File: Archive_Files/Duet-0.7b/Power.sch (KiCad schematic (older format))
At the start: 22 parts, among them U2 TC2117-3.3VDBTR, U3 MC7805CDTG

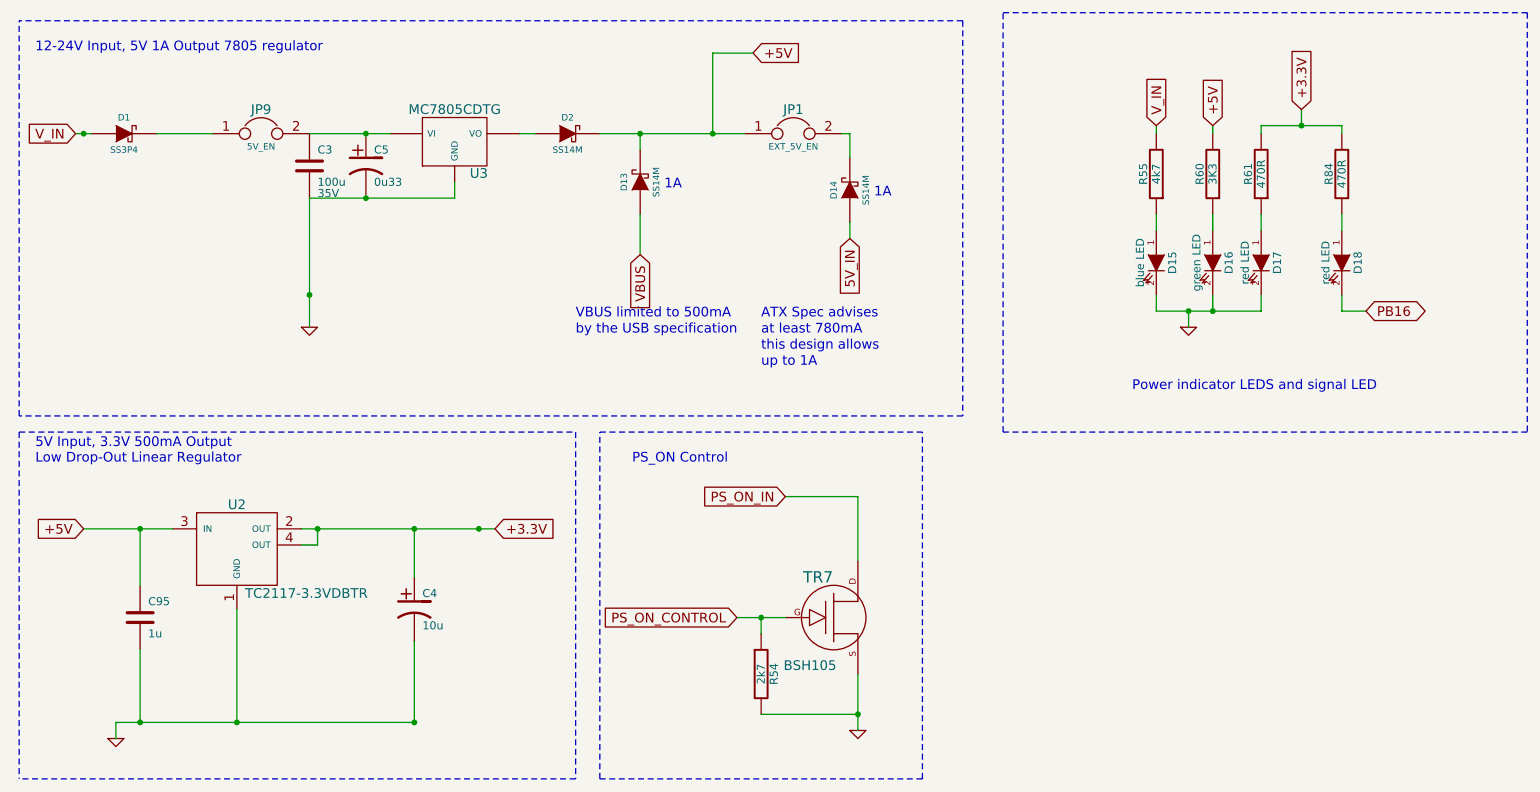
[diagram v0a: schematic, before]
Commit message: Tony's suggestion of re-instating the external 5V supply implemented. Power LEDS more widely spaced to allow easier access by printed light-pipe.
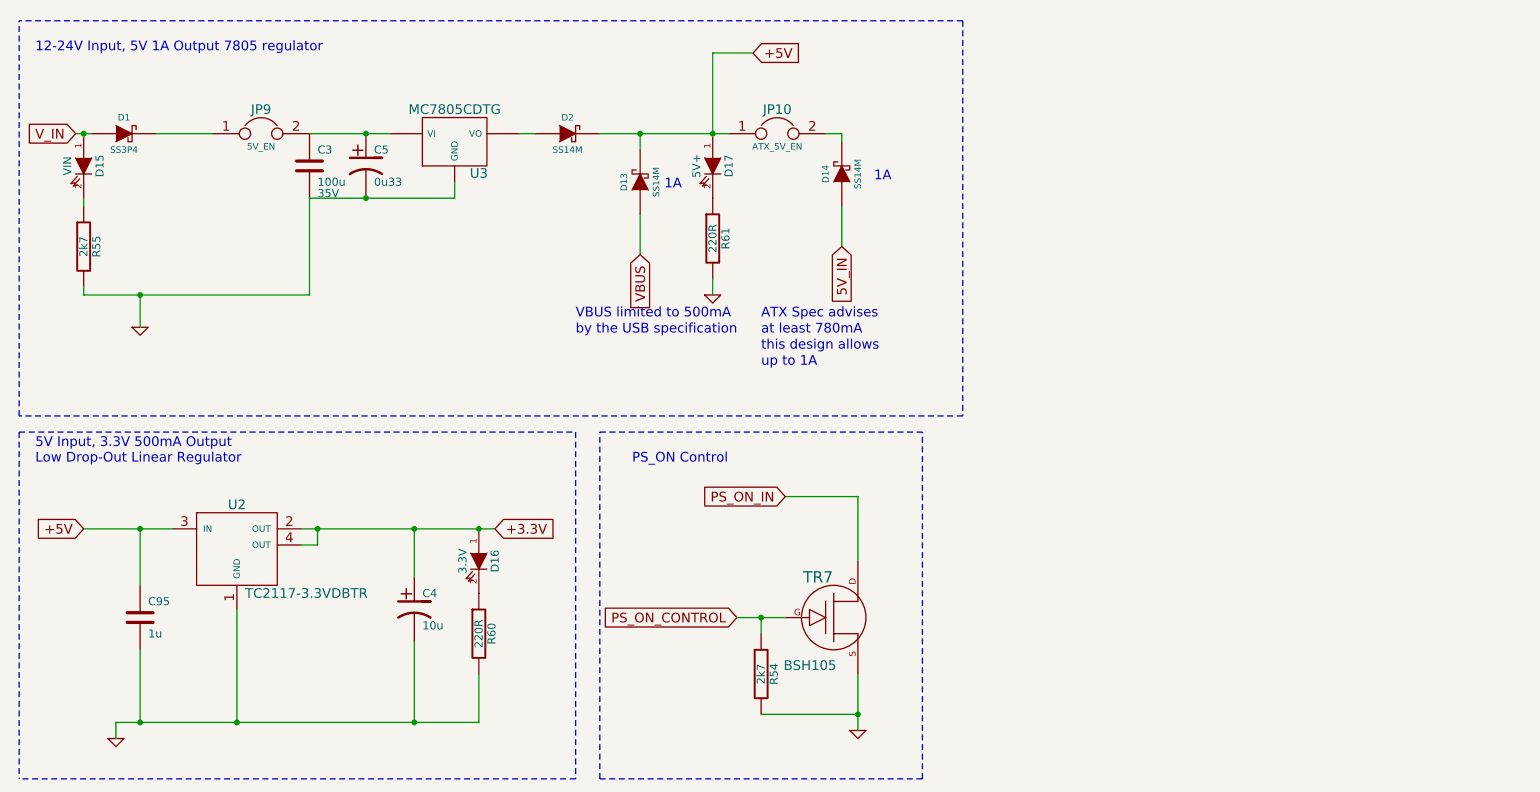
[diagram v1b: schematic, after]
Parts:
- removed D18: red LED, symbol LED
- removed JP1: EXT_5V_EN, symbol JUMPER
- removed R84: 470R, symbol R
- added JP10: ATX_5V_EN, symbol JUMPER
- D15: value blue LED -> VIN
- D16: value green LED -> 3.3V
- D17: value red LED -> 5V+
- R55: value 4k7 -> 2k7
- R60: value 3K3 -> 220R
- R61: value 470R -> 220R
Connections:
- net +3.3V: now also D16.1 (A); no longer R61.2
- net +5V: now also D17.1 (A), JP10.1; no longer R60.2
- net GND: now also R55.2, R60.2, R61.2; no longer D15.2 (K), D16.2 (K), D17.2 (K)
- net V_IN: now also D15.1 (A); no longer R55.2
- net at R55.1: now also D15.2 (K); no longer D15.1 (A)
- net at R60.1: now also D16.2 (K); no longer D16.1 (A)
- net at R61.1: now also D17.2 (K); no longer D17.1 (A)
- net at D14.2 (K): now also JP10.2
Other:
- note removed: "Power indicator LEDS and signal LED"
